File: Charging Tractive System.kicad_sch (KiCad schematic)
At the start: 7 parts, among them SW1 SW_Push_Open

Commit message: update
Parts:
- 15kΩ: value TSMP1 -> TSMP-
- 15kΩ: value TSMP2 -> TSMP+
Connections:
- new net: 15kΩ.2, HK-LF-312-20. (Null_Line) (x2)
- now unconnected: 15kΩ.1, 15kΩ.1
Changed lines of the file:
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@@
-	)
-	(junction
-		(at 138.43 43.18)
-		(diameter 0)
-		(color 0 0 0 0)
 	)
 	(junction
@@
 	)
 	(junction
-		(at 137.16 45.72)
+		(at 138.43 45.72)
 		(diameter 0)
 		(color 0 0 0 0)
 	)
-	(junction
-		(at 125.73 45.72)
-		(diameter 0)
-		(color 0 0 0 0)
+	(wire
+		(pts
+			(xy 138.43 21.59) (xy 138.43 31.75)
+		)
+		(stroke
+			(width 0)
+			(type default)
+		)
 	)
 	(wire
@@
 	(wire
 		(pts
-			(xy 137.16 45.72) (xy 162.56 45.72)
+			(xy 118.11 45.72) (xy 138.43 45.72)
 		)
 		(stroke
@@
 	(wire
 		(pts
+			(xy 127 21.59) (xy 127 31.75)
+		)
+		(stroke
+			(width 0)
+			(type default)
+		)
+	)
+	(wire
+		(pts
 			(xy 106.68 109.22) (xy 151.13 109.22)
 		)
@@
 	(wire
 		(pts
-			(xy 138.43 43.18) (xy 162.56 43.18)
+			(xy 127 43.18) (xy 162.56 43.18)
 		)
 		(stroke
@@
 	(wire
 		(pts
+			(xy 138.43 45.72) (xy 162.56 45.72)
+		)
+		(stroke
+			(width 0.508)
+			(type default)
+		)
+	)
+	(wire
+		(pts
 			(xy 135.89 58.42) (xy 162.56 58.42)
 		)
@@
 	(wire
 		(pts
-			(xy 137.16 31.75) (xy 137.16 45.72)
-		)
-		(stroke
-			(width 0)
-			(type default)
-		)
-	)
-	(wire
-		(pts
 			(xy 162.56 81.28) (xy 143.51 81.28)
 		)
@@
 	(wire
 		(pts
-			(xy 138.43 31.75) (xy 137.16 31.75)
-		)
-		(stroke
-			(width 0)
-			(type default)
-		)
-	)
-	(wire
-		(pts
 			(xy 135.89 60.96) (xy 162.56 60.96)
 		)
@@
 	(wire
 		(pts
-			(xy 118.11 45.72) (xy 125.73 45.72)
+			(xy 127 63.5) (xy 135.89 63.5)
+		)
+		(stroke
+			(width 0)
+			(type default)
+		)
+	)
+	(wire
+		(pts
+			(xy 127 55.88) (xy 135.89 55.88)
+		)
+		(stroke
+			(width 0)
+			(type default)
+		)
+	)
+	(wire
+		(pts
+			(xy 118.11 78.74) (xy 162.56 78.74)
 		)
 		(stroke
@@
 	(wire
 		(pts
-			(xy 125.73 45.72) (xy 137.16 45.72)
+			(xy 153.67 83.82) (xy 162.56 83.82)
+		)
+		(stroke
+			(width 0)
+			(type default)
+		)
+	)
+	(wire
+		(pts
+			(xy 106.68 114.3) (xy 151.13 114.3)
 		)
 		(stroke
@@
 	(wire
 		(pts
-			(xy 127 63.5) (xy 135.89 63.5)
-		)
-		(stroke
-			(width 0)
-			(type default)
-		)
-	)
-	(wire
-		(pts
-			(xy 127 31.75) (xy 125.73 31.75)
-		)
-		(stroke
-			(width 0)
-			(type default)
-		)
-	)
-	(wire
-		(pts
-			(xy 127 55.88) (xy 135.89 55.88)
-		)
-		(stroke
-			(width 0)
-			(type default)
-		)
-	)
-	(wire
-		(pts
-			(xy 138.43 39.37) (xy 138.43 43.18)
-		)
-		(stroke
-			(width 0)
-			(type default)
-		)
-	)
-	(wire
-		(pts
-			(xy 118.11 78.74) (xy 162.56 78.74)
+			(xy 135.89 55.88) (xy 135.89 58.42)
+		)
+		(stroke
+			(width 0)
+			(type default)
+		)
+	)
+	(wire
+		(pts
+			(xy 118.11 76.2) (xy 162.56 76.2)
 		)
 		(stroke
@@
 	(wire
 		(pts
-			(xy 153.67 83.82) (xy 162.56 83.82)
-		)
-		(stroke
-			(width 0)
-			(type default)
-		)
-	)
-	(wire
-		(pts
-			(xy 106.68 114.3) (xy 151.13 114.3)
+			(xy 118.11 73.66) (xy 162.56 73.66)
 		)
 		(stroke
@@
 	(wire
 		(pts
-			(xy 135.89 55.88) (xy 135.89 58.42)
-		)
-		(stroke
-			(width 0)
-			(type default)
-		)
-	)
-	(wire
-		(pts
-			(xy 118.11 76.2) (xy 162.56 76.2)
-		)
-		(stroke
-			(width 0.508)
-			(type default)
-		)
-	)
-	(wire
-		(pts
-			(xy 118.11 73.66) (xy 162.56 73.66)
-		)
-		(stroke
-			(width 0.508)
-			(type default)
-		)
-	)
-	(wire
-		(pts
-			(xy 125.73 31.75) (xy 125.73 45.72)
-		)
-		(stroke
-			(width 0)
-			(type default)
-		)
-	)
-	(wire
-		(pts
 			(xy 160.02 63.5) (xy 160.02 66.04)
 		)
@@
 	(wire
 		(pts
+			(xy 138.43 39.37) (xy 138.43 45.72)
+		)
+		(stroke
+			(width 0)
+			(type default)
+		)
+	)
+	(wire
+		(pts
 			(xy 143.51 81.28) (xy 143.51 83.82)
 		)
@@
 		(stroke
 			(width 0)
-			(type default)
-		)
-	)
-	(wire
-		(pts
-			(xy 127 43.18) (xy 138.43 43.18)
-		)
-		(stroke
-			(width 0.508)
 			(type default)
 		)
@@
 			)
 		)
-		(property "Value" "TSMP1"
+		(property "Value" "TSMP-"
 			(at 140.97 36.8299 0)
 			(effects
@@
 			)
 		)
-		(property "Value" "TSMP2"
+		(property "Value" "TSMP+"
 			(at 129.54 36.8299 0)
 			(effects

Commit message: add AIR (accumulator isolation relay)
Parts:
- added BT1: HVBattery, symbol Device:Battery
- added F1: AccumulatorFuse, symbol Device:Fuse
- added K1: AIR2, Relay_THT:Relay_SPST-NO_Fujitsu_FTR-LYAA005x_FormA_Vertical, symbol Relay:Fujitsu_FTR-LYAA005x
- added K2: AIR1, Relay_THT:Relay_SPST-NO_Fujitsu_FTR-LYAA005x_FormA_Vertical, symbol Relay:Fujitsu_FTR-LYAA005x
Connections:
- new net: F1.2, iso175. (V-)
- new net: BT1.2 (-), iso175. (V-)
- new net: BT1.1 (+), K1.13, K2.14
- new net: F1.1, K1.14
- new net GLV: K1.A1, K2.A1
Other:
- note added: "Precharge"
- note added: "Precharge Control"
- moved on the sheet: Orion2, iso175

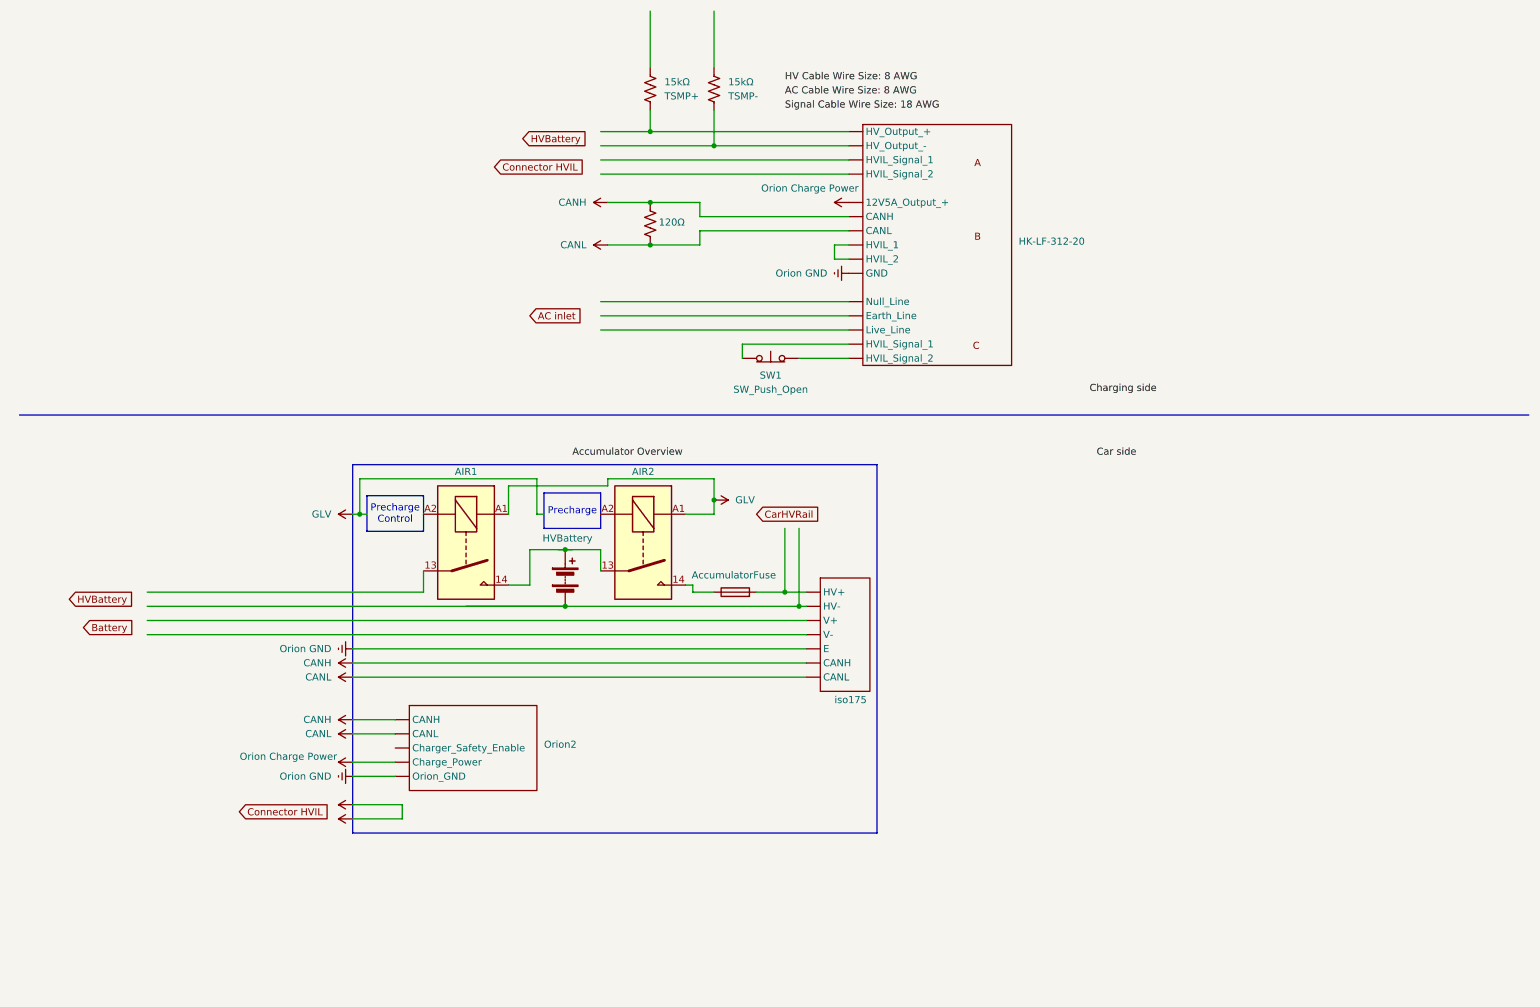
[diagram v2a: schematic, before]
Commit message: update to charging system with Esmeralda CTS
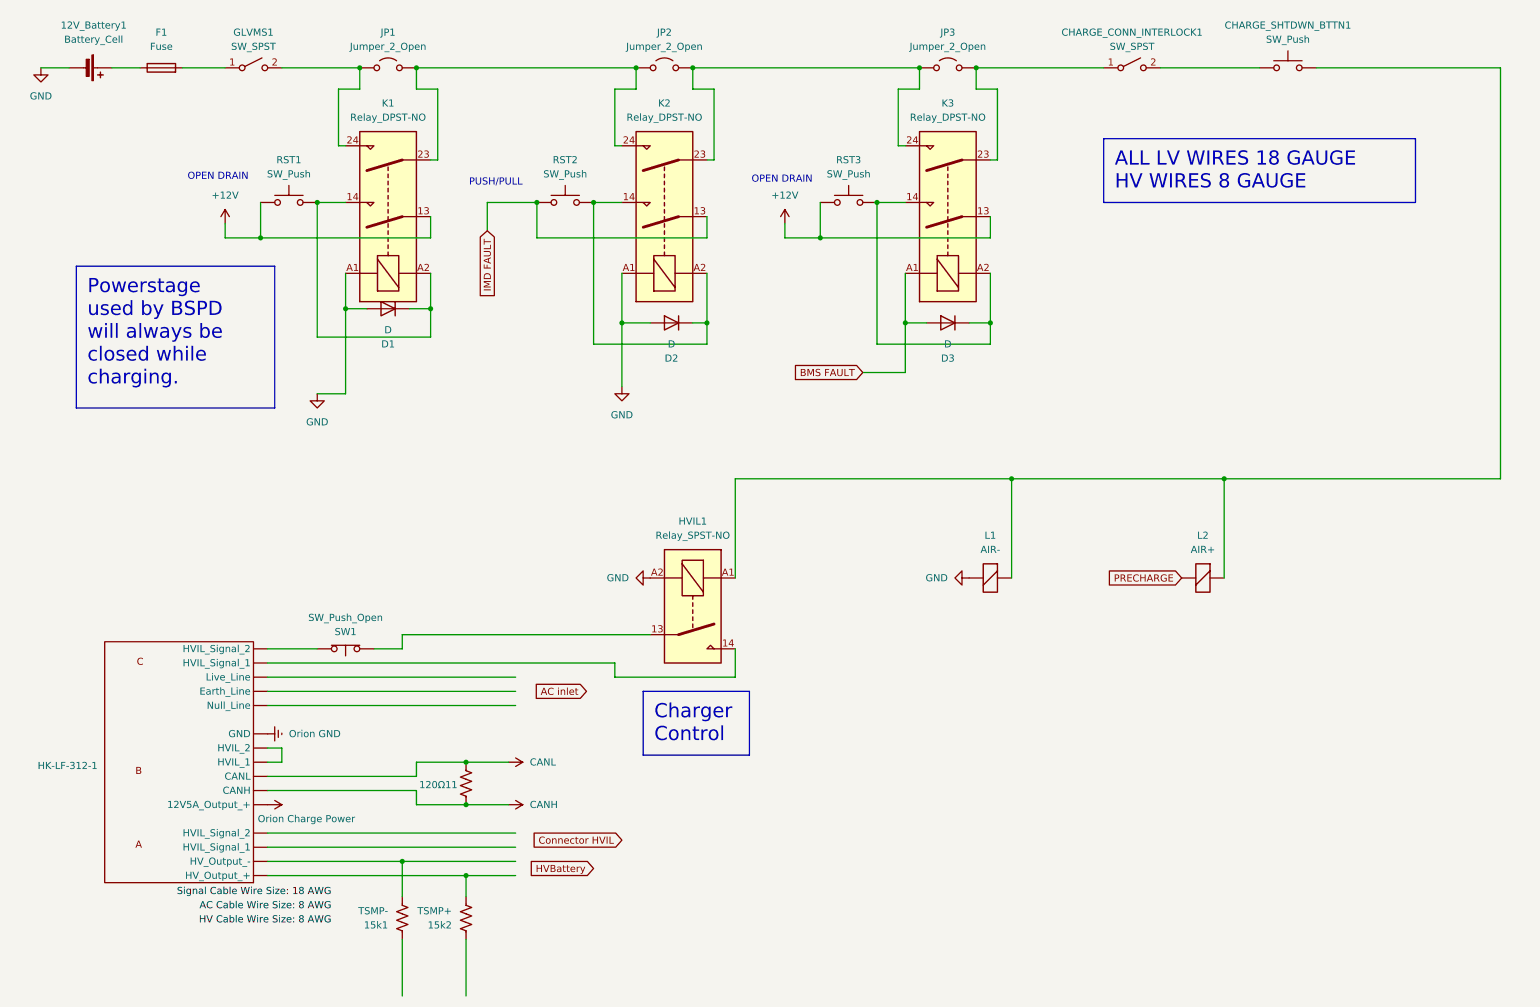
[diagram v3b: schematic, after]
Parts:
- removed 120Ω: R_US, symbol Device:R_US
- removed 15kΩ: TSMP-, symbol Device:R_US
- removed 15kΩ: TSMP+, symbol Device:R_US
- removed BT1: HVBattery, symbol Device:Battery
- removed HK-LF-312-20: ~, symbol Charging Tractive System:HK-LF-540-12
- removed K1: AIR2, Relay_THT:Relay_SPST-NO_Fujitsu_FTR-LYAA005x_FormA_Vertical, symbol Relay:Fujitsu_FTR-LYAA005x
- removed K2: AIR1, Relay_THT:Relay_SPST-NO_Fujitsu_FTR-LYAA005x_FormA_Vertical, symbol Relay:Fujitsu_FTR-LYAA005x
- removed Orion2: ~, symbol Charging Tractive System:Orion_2
- removed iso175: ~, symbol Charging Tractive System:iso175
- added 120Ω11: R_US, symbol Device:R_US
- added 12V_Battery1: Battery_Cell, symbol Device:Battery_Cell
- added 15k1: TSMP-, symbol Device:R_US
- added 15k2: TSMP+, symbol Device:R_US
- added CHARGE_CONN_INTERLOCK1, GLVMS1: SW_SPST, symbol Switch:SW_SPST
- added CHARGE_SHTDWN_BTTN1, RST1, RST2, RST3: SW_Push, symbol Switch:SW_Push
- added D1, D2, D3: D, symbol Device:D
- added HK-LF-312-1: ~, symbol Charging Tractive System:HK-LF-540-12
- added HVIL1: Relay_SPST-NO, symbol Relay:Relay_SPST-NO
- added JP1, JP2, JP3: Jumper_2_Open, symbol Jumper:Jumper_2_Open
- added K1, K2, K3: Relay_DPST-NO, symbol Relay:Relay_DPST-NO
- added L1: AIR-, symbol Device:ElectromagneticActor
- added L2: AIR+, symbol Device:ElectromagneticActor
- F1: value AccumulatorFuse -> Fuse
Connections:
- net CANH: now also 120Ω11.1, HK-LF-312-1. (Null_Line)
- net CANL: now also 120Ω11.2, HK-LF-312-1. (Null_Line)
- net Orion Charge Power: now also HK-LF-312-1. (Null_Line)
- net Orion GND: now also HK-LF-312-1. (Null_Line)
- net at F1.2: now also GLVMS1.1 (A)
- net at F1.1: now also 12V_Battery1.1 (+)
- net at SW1.1 (A): now also HVIL1.13
- net at SW1.2 (B): now also HK-LF-312-1. (Null_Line)
- new net: HK-LF-312-1. (Null_Line), HVIL1.14
- new net: 15k1.2, HK-LF-312-1. (Null_Line)
- new net: 15k2.2, HK-LF-312-1. (Null_Line)
- new net: JP2.2 (B), JP3.1 (A), K2.23, K3.24
- new net: CHARGE_CONN_INTERLOCK1.1 (A), JP3.2 (B), K3.23
- new net: D2.1 (K), K2.14, K2.A2, RST2.2
- new net: CHARGE_SHTDWN_BTTN1.2, HVIL1.A1, L1.1 (-), L2.1 (-)
- new net: D1.1 (K), K1.14, K1.A2, RST1.2
- new net: D3.1 (K), K3.14, K3.A2, RST3.2
- new net: JP1.2 (B), JP2.1 (A), K1.23, K2.24
- new net: GLVMS1.2 (B), JP1.1 (A), K1.24
- new net: CHARGE_CONN_INTERLOCK1.2 (B), CHARGE_SHTDWN_BTTN1.1
- new net +12V: K1.13, K3.13, RST1.1, RST3.1
- new net BMS FAULT: D3.2 (A), K3.A1
- new net GND: 12V_Battery1.2 (-), D1.2 (A), D2.2 (A), HVIL1.A2, K1.A1, K2.A1, L1.2 (+)
- new net IMD FAULT: K2.13, RST2.1
- new net PRECHARGE: L2.2 (+)
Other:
- note added: "OPEN DRAIN"
- note added: "PUSH/PULL"
- note removed: "Precharge"
- note removed: "Precharge Control"
